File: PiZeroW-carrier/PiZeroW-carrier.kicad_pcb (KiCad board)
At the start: 2 copper layers, 65 x 30 mm, 26 parts, among them CON1 BARREL_JACK, J1 PI40HAT, P1 USB_OTG, SW1 SW_PUSH, U1 BA50BC0WFP-E2CT, U2 BA06CC0WFP-E2CT

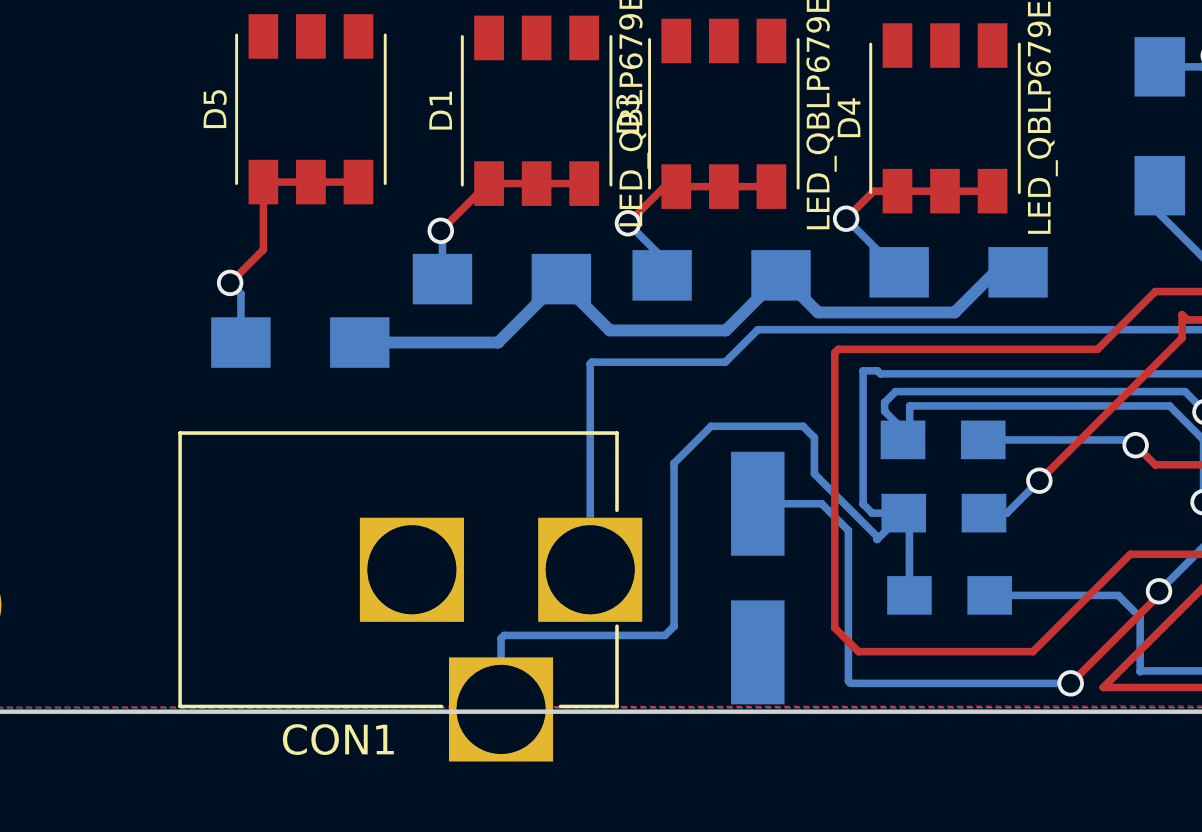
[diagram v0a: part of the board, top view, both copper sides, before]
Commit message: Fix of Copper Pour and Placement of the Barrel Jack
Fixed the Copper Pour from the last Push and Re positioned the Barrel Jack
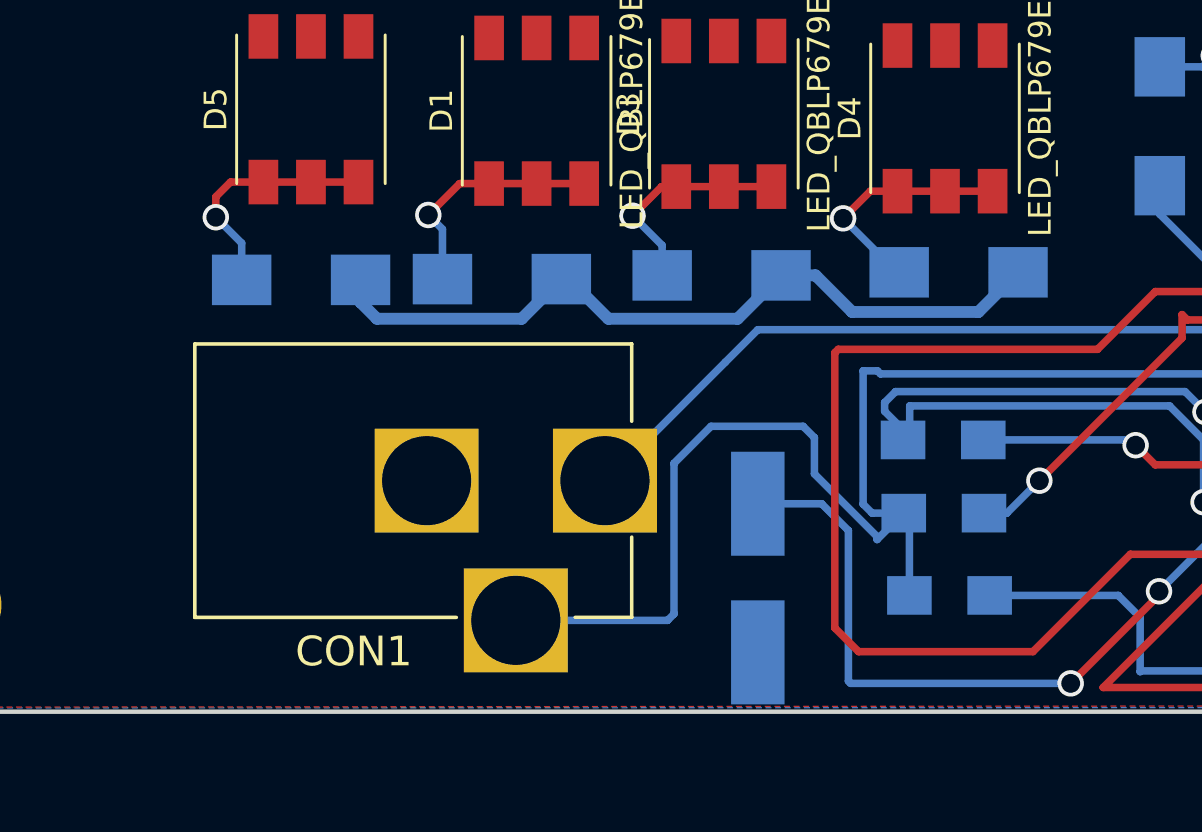
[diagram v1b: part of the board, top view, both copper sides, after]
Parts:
- moved CON1 3.04 mm to (134.8, 101.7)
- moved R8 2.11 mm to (124.6, 95.0)
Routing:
- net +BATT: track 77.4 -> 71.6 mm
- net GND: track 51.7 -> 48.3 mm
- net /Leds/+6V: track 26.0 -> 27.1 mm
- net Net-(D5-Pad4): track 9.21 -> 8.16 mm
- net Net-(D1-Pad4): track 7.13 -> 8.04 mm

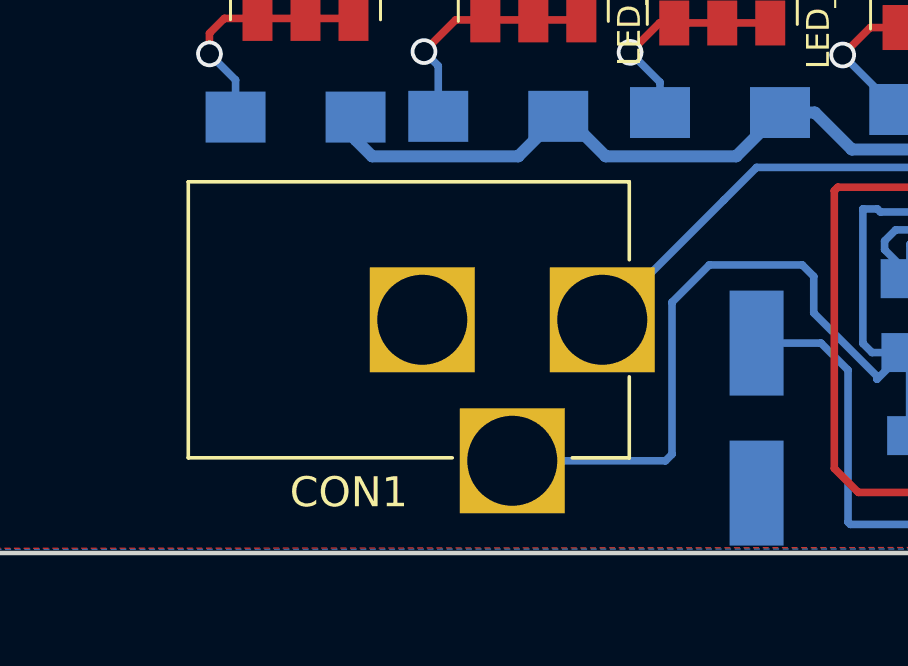
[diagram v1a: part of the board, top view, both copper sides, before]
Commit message: Updated Camera Hole Size and moved barrel jack
Update of the Hole for the camera and placement of the Barrel Jack
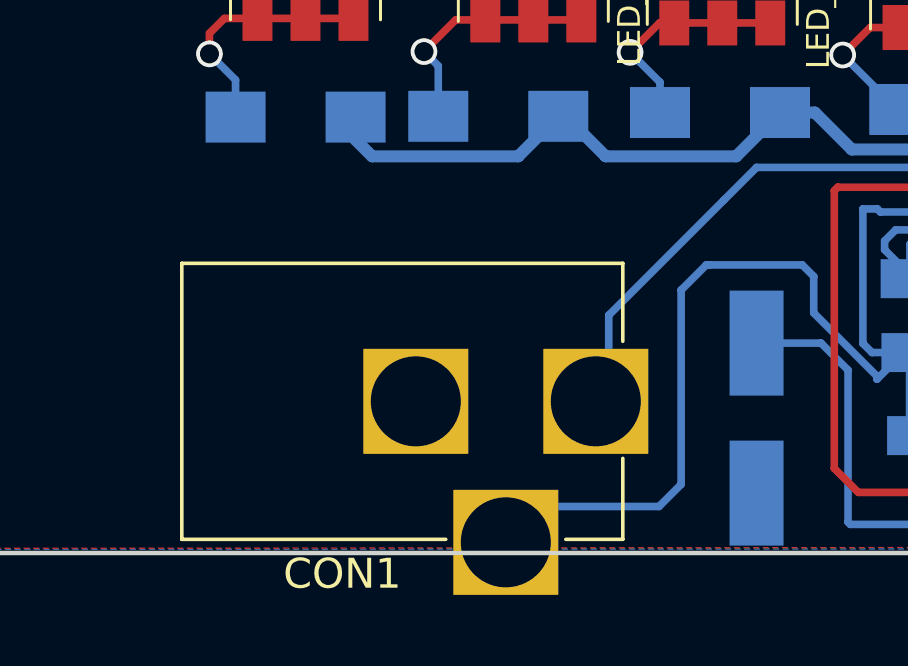
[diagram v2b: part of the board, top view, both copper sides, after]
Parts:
- moved CON1 2.73 mm to (134.6, 104.4)
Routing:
- net +BATT: track 71.6 -> 74.4 mm
- net GND: track 48.3 -> 50.5 mm
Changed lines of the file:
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@@
     (links 64)
     (no_connects 16)
-    (area 109.424999 79.424999 174.575001 109.575001)
+    (area 107.133143 79.190999 178.224 109.829602)
     (thickness 1.6)
     (drawings 13)
-    (tracks 178)
+    (tracks 181)
     (zones 0)
     (modules 26)
@@
   )
   (module Connectors:BARREL_JACK (layer F.Cu)
-    (at 134.8359 101.727)
+    (at 134.62 104.4448)
     (descr "DC Barrel Jack")
     (tags "Power Jack")
@@
   (gr_arc (start 171.5 82.5) (end 171.5 79.5) (angle 90) (layer Edge.Cuts) (width 0.15))
   (gr_arc (start 112.5 82.5) (end 109.5 82.5) (angle 90) (layer Edge.Cuts) (width 0.15))
-  (segment (start 137.16 101.1428) (end 137.16 106.2101) (width 0.254) (layer B.Cu) (net 1))
-  (segment (start 137.16 106.2101) (end 136.9431 106.427) (width 0.254) (layer B.Cu) (net 1))
-  (segment (start 136.9431 106.427) (end 131.8359 106.427) (width 0.254) (layer B.Cu) (net 1))
+  (segment (start 138.4046 99.8982) (end 138.303 99.8982) (width 0.254) (layer B.Cu) (net 1))
+  (segment (start 141.5034 99.8982) (end 138.4046 99.8982) (width 0.254) (layer B.Cu) (net 1))
+  (segment (start 141.8844 100.2792) (end 141.5034 99.8982) (width 0.254) (layer B.Cu) (net 1))
+  (segment (start 141.8844 101.4984) (end 141.8844 100.2792) (width 0.254) (layer B.Cu) (net 1))
+  (segment (start 143.9926 103.6066) (end 141.8844 101.4984) (width 0.254) (layer B.Cu) (net 1))
+  (segment (start 143.9926 103.7082) (end 143.9926 103.6066) (width 0.254) (layer B.Cu) (net 1))
+  (segment (start 144.8816 102.8192) (end 143.9926 103.7082) (width 0.254) (layer B.Cu) (net 1))
+  (segment (start 136.7282 107.95) (end 132.8148 107.95) (width 0.254) (layer B.Cu) (net 1))
+  (segment (start 137.4648 107.2134) (end 136.7282 107.95) (width 0.254) (layer B.Cu) (net 1))
+  (segment (start 137.4648 100.7364) (end 137.4648 107.2134) (width 0.254) (layer B.Cu) (net 1))
+  (segment (start 138.303 99.8982) (end 137.4648 100.7364) (width 0.254) (layer B.Cu) (net 1))
+  (segment (start 132.8148 107.95) (end 131.62 109.1448) (width 0.254) (layer B.Cu) (net 1))
   (segment (start 143.5227 98.0313) (end 144.0053 98.0313) (width 0.254) (layer B.Cu) (net 1))
   (segment (start 144.0053 98.0313) (end 144.1069 98.1329) (width 0.254) (layer B.Cu) (net 1))
   (segment (start 144.8905 102.8192) (end 144.8816 102.8192) (width 0.254) (layer B.Cu) (net 1))
-  (segment (start 144.8816 102.8192) (end 143.9926 103.7082) (width 0.254) (layer B.Cu) (net 1))
-  (segment (start 143.9926 103.7082) (end 143.9926 103.6066) (width 0.254) (layer B.Cu) (net 1))
-  (segment (start 143.9926 103.6066) (end 141.8844 101.4984) (width 0.254) (layer B.Cu) (net 1))
-  (segment (start 141.8844 101.4984) (end 141.8844 100.2792) (width 0.254) (layer B.Cu) (net 1))
-  (segment (start 141.8844 100.2792) (end 141.5034 99.8982) (width 0.254) (layer B.Cu) (net 1))
-  (segment (start 141.5034 99.8982) (end 138.4046 99.8982) (width 0.254) (layer B.Cu) (net 1))
-  (segment (start 138.4046 99.8982) (end 137.16 101.1428) (width 0.254) (layer B.Cu) (net 1))
   (segment (start 158.325 102.235) (end 158.325 101.9361) (width 0.254) (layer B.Cu) (net 1))
   (segment (start 144.8905 102.8192) (end 143.8275 102.8192) (width 0.254) (layer B.Cu) (net 1))
@@
   (segment (start 167.4622 95.25) (end 170.735 95.25) (width 0.254) (layer B.Cu) (net 3))
   (segment (start 167.4114 95.1992) (end 167.4622 95.25) (width 0.254) (layer B.Cu) (net 3))
-  (segment (start 134.8359 101.727) (end 134.8994 101.727) (width 0.254) (layer B.Cu) (net 4))
-  (segment (start 134.8994 101.727) (end 138.8872 97.7392) (width 0.254) (layer B.Cu) (net 4))
+  (segment (start 138.8872 97.7392) (end 135.0518 101.5746) (width 0.254) (layer B.Cu) (net 4))
+  (segment (start 144.8651 100.0087) (end 144.2466 99.3902) (width 0.254) (layer B.Cu) (net 4))
+  (segment (start 144.2466 99.3902) (end 144.2466 99.098102) (width 0.254) (layer B.Cu) (net 4))
+  (segment (start 144.2466 99.098102) (end 144.614902 98.7298) (width 0.254) (layer B.Cu) (net 4))
+  (segment (start 144.614902 98.7298) (end 154.3558 98.7298) (width 0.254) (layer B.Cu) (net 4))
+  (segment (start 154.3558 98.7298) (end 155.0416 99.4156) (width 0.254) (layer B.Cu) (net 4))
+  (via (at 155.0416 99.4156) (size 0.889) (drill 0.635) (layers F.Cu B.Cu) (net 4))
+  (segment (start 155.0416 99.4156) (end 155.6512 98.806) (width 0.254) (layer F.Cu) (net 4))
+  (segment (start 155.6512 98.806) (end 155.6512 97.2566) (width 0.254) (layer F.Cu) (net 4))
+  (via (at 155.6512 97.2566) (size 0.889) (drill 0.635) (layers F.Cu B.Cu) (net 4))
+  (segment (start 155.6512 97.2566) (end 155.0416 96.647) (width 0.254) (layer B.Cu) (net 4))
+  (segment (start 155.0416 96.647) (end 139.9794 96.647) (width 0.254) (layer B.Cu) (net 4))
+  (segment (start 139.9794 96.647) (end 138.8872 97.7392) (width 0.254) (layer B.Cu) (net 4))
+  (segment (start 135.0518 101.5746) (end 135.0518 104.013) (width 0.254) (layer B.Cu) (net 4) (status 800000))
+  (segment (start 135.0518 104.013) (end 134.62 104.4448) (width 0.254) (layer B.Cu) (net 4) (status C00000))
   (segment (start 158.0007 97.2566) (end 158.0007 98.3488) (width 0.254) (layer F.Cu) (net 4))
   (segment (start 158.0007 98.3488) (end 157.6705 98.679) (width 0.254) (layer F.Cu) (net 4))
@@
   (via (at 158.0007 97.2566) (size 0.889) (drill 0.635) (layers F.Cu B.Cu) (net 4))
   (segment (start 144.8651 100.3554) (end 144.8651 100.0087) (width 0.254) (layer B.Cu) (net 4))
-  (segment (start 144.8651 100.0087) (end 144.2466 99.3902) (width 0.254) (layer B.Cu) (net 4))
-  (segment (start 144.2466 99.3902) (end 144.2466 99.098102) (width 0.254) (layer B.Cu) (net 4))
-  (segment (start 144.2466 99.098102) (end 144.614902 98.7298) (width 0.254) (layer B.Cu) (net 4))
-  (segment (start 144.614902 98.7298) (end 154.3558 98.7298) (width 0.254) (layer B.Cu) (net 4))
-  (segment (start 154.3558 98.7298) (end 155.0416 99.4156) (width 0.254) (layer B.Cu) (net 4))
-  (via (at 155.0416 99.4156) (size 0.889) (drill 0.635) (layers F.Cu B.Cu) (net 4))
-  (segment (start 155.0416 99.4156) (end 155.6512 98.806) (width 0.254) (layer F.Cu) (net 4))
-  (segment (start 155.6512 98.806) (end 155.6512 97.2566) (width 0.254) (layer F.Cu) (net 4))
-  (via (at 155.6512 97.2566) (size 0.889) (drill 0.635) (layers F.Cu B.Cu) (net 4))
-  (segment (start 155.6512 97.2566) (end 155.0416 96.647) (width 0.254) (layer B.Cu) (net 4))
-  (segment (start 155.0416 96.647) (end 139.9794 96.647) (width 0.254) (layer B.Cu) (net 4))
-  (segment (start 139.9794 96.647) (end 138.8872 97.7392) (width 0.254) (layer B.Cu) (net 4))
   (segment (start 145.0899 99.2124) (end 145.0899 100.1306) (width 0.254) (layer B.Cu) (net 4))
   (segment (start 145.0899 100.1306) (end 144.8651 100.3554) (width 0.254) (layer B.Cu) (net 4))
@@
     )
   )
-  (zone (net 0) (net_name "") (layer F.Cu) (hatch none 0.508)
+  (zone (net 0) (net_name "") (layer F.Cu) (hatch edge 0.508)
     (connect_pads (clearance 0.508))
     (min_thickness 0.254)
@@
     (polygon
       (pts
-        (xy 120.8278 99.822) (xy 110.5662 99.822) (xy 110.5662 86.3346) (xy 120.8278 86.3346)
+        (xy 120 98) (xy 111 98) (xy 111 89) (xy 120 89)
       )
     )
   )
-  (zone (net 0) (net_name "") (layer B.Cu) (hatch none 0.508)
+  (zone (net 0) (net_name "") (layer B.Cu) (hatch edge 0.508)
     (connect_pads (clearance 0.508))
     (min_thickness 0.254)
@@
     (polygon
       (pts
-        (xy 120.8278 99.822) (xy 110.5662 99.822) (xy 110.5662 86.3346) (xy 120.8278 86.3346)
+        (xy 119.9896 97.9932) (xy 110.998 97.9932) (xy 110.998 89.0016) (xy 119.9896 89.0016)
       )
     )

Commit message: this could work
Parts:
- moved SW1 42.3 mm to (119.7, 104.7)
- moved R1 41.7 mm to (113.3, 100.8), turned to 0 degrees
- moved CON1 15.7 mm to (144.8, 92.5), turned to 180 degrees
- moved D1 10.6 mm to (122.1, 91.1)
- moved D4 10.6 mm to (135.9, 91.4)
- moved R7 10.6 mm to (136.3, 96.6)
- moved D5 10.6 mm to (114.5, 91.1)
- moved D3 10.6 mm to (128.4, 91.2)
- moved R4 10.6 mm to (121.0, 96.8)
- moved R6 10.6 mm to (128.3, 96.7)
- moved R8 10.6 mm to (114.2, 96.8)
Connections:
- D6 pad 1: /Power/+5V -> (no net)
- J1 pad 1: /raspberrypi-gpio-40pin/P3V3_HAT -> (no net)
- J1 pad 10: Net-(J1-Pad10) -> (no net)
- J1 pad 12: Net-(J1-Pad12) -> (no net)
- J1 pad 13: /Power/PiDisable -> (no net)
- J1 pad 15: Net-(J1-Pad15) -> (no net)
- J1 pad 16: Net-(J1-Pad16) -> (no net)
- J1 pad 17: Net-(J1-Pad17) -> (no net)
- J1 pad 18: Net-(J1-Pad18) -> (no net)
- J1 pad 19: Net-(J1-Pad19) -> (no net)
- J1 pad 21: Net-(J1-Pad21) -> (no net)
- J1 pad 22: Net-(J1-Pad22) -> (no net)
- J1 pad 23: Net-(J1-Pad23) -> (no net)
- J1 pad 24: Net-(J1-Pad24) -> (no net)
- J1 pad 26: Net-(J1-Pad26) -> (no net)
- J1 pad 27: /raspberrypi-gpio-40pin/SDA -> (no net)
- J1 pad 28: /raspberrypi-gpio-40pin/SCL -> (no net)
- J1 pad 29: Net-(J1-Pad29) -> (no net)
- J1 pad 3: Net-(J1-Pad3) -> (no net)
- J1 pad 31: Net-(J1-Pad31) -> (no net)
- J1 pad 32: Net-(J1-Pad32) -> (no net)
- J1 pad 33: Net-(J1-Pad33) -> (no net)
- J1 pad 35: Net-(J1-Pad35) -> (no net)
- J1 pad 36: Net-(J1-Pad36) -> (no net)
- J1 pad 37: Net-(J1-Pad37) -> (no net)
- J1 pad 38: Net-(J1-Pad38) -> (no net)
- J1 pad 40: Net-(J1-Pad40) -> (no net)
- J1 pad 5: Net-(J1-Pad5) -> (no net)
- J1 pad 7: Net-(J1-Pad7) -> (no net)
- J1 pad 8: Net-(J1-Pad8) -> (no net)
- R12 pad 1: +5V -> (no net)
- U2 pad 4: /Power/+6V -> (no net)
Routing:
- net Net-(R2-Pad1): track 77.0 -> 16.4 mm
- net +BATT: track 74.4 -> 18.7 mm, vias 6 -> 1
- net GND: track 50.5 -> 26.9 mm
- net Net-(R1-Pad2): track 10.6 -> 0.00 mm, vias 1 -> 0
- net (no net): track 0.00 -> 0.51 mm
